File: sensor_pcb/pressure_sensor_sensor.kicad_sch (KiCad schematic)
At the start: 12 parts, among them J1 Conn_01x01_Pin, J10 Conn_01x02_Pin, J12 Conn_01x01_Pin, J13 Conn_01x01_Pin, J14 Conn_01x01_Pin, J15 Conn_01x01_Pin, J16 Conn_01x01_Pin, J17 Conn_01x01_Pin, J18 Conn_01x01_Pin, J7 Conn_01x02_Pin, J8 Conn_01x02_Pin, J9 Conn_01x02_Pin

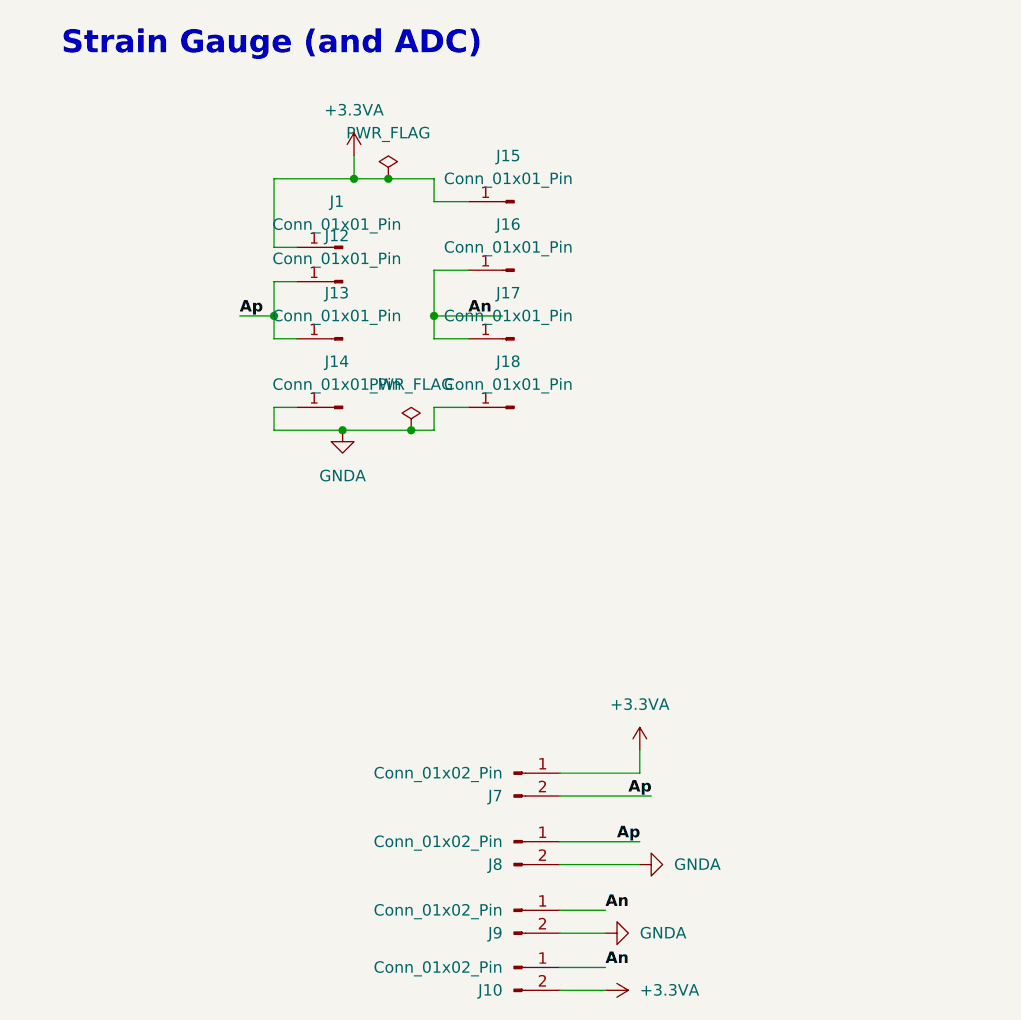
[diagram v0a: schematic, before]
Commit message: mounting_holes_added
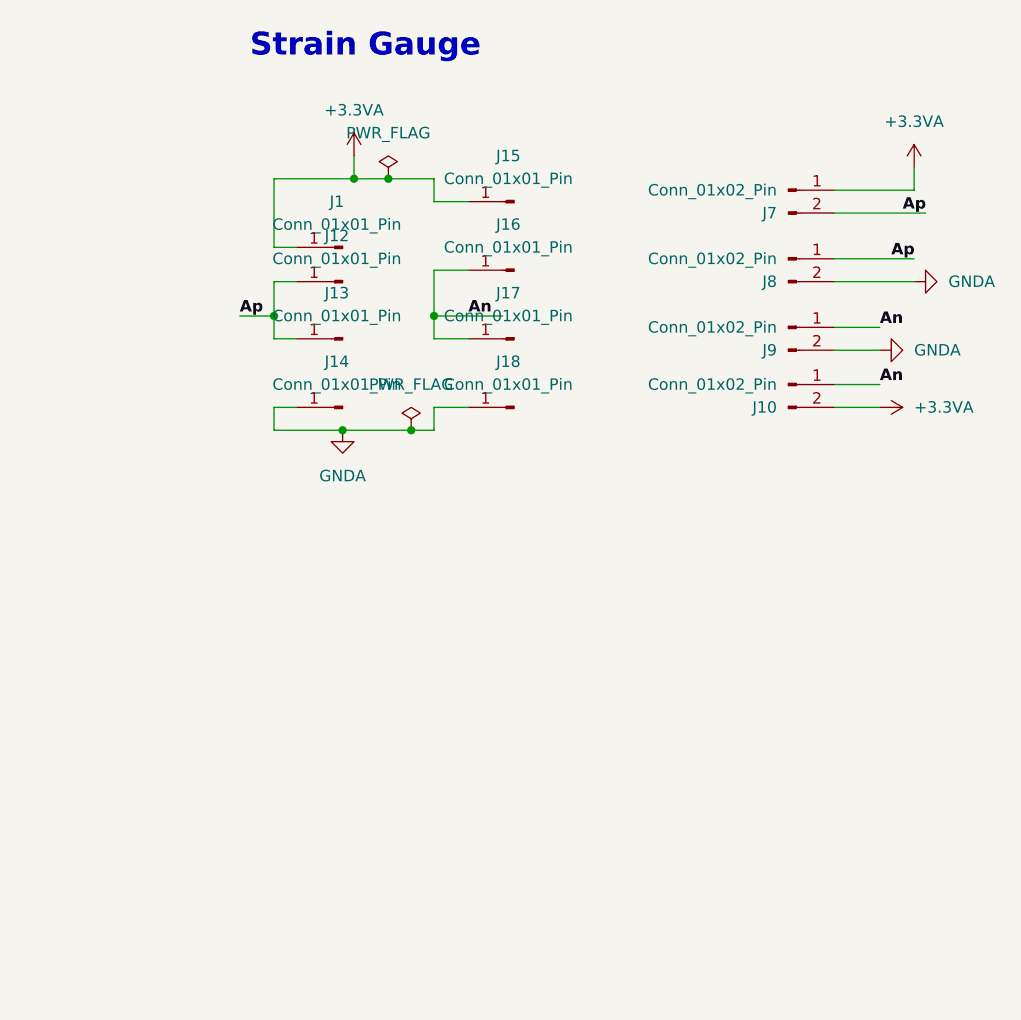
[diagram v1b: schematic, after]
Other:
- note added: "Strain Gauge"
- note removed: "Strain Gauge (and ADC)"
- moved on the sheet: J10, J7, J8, J9
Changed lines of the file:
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@@
 	(wire
 		(pts
-			(xy 205.74 97.79) (xy 214.63 97.79)
-		)
-		(stroke
-			(width 0)
-			(type default)
-		)
-	)
-	(wire
-		(pts
-			(xy 205.74 107.95) (xy 214.63 107.95)
+			(xy 236.22 33.02) (xy 245.11 33.02)
+		)
+		(stroke
+			(width 0)
+			(type default)
+		)
+	)
+	(wire
+		(pts
+			(xy 236.22 43.18) (xy 245.11 43.18)
 		)
 		(stroke
@@
 	(wire
 		(pts
-			(xy 205.74 100.33) (xy 215.9 100.33)
+			(xy 236.22 35.56) (xy 246.38 35.56)
 		)
 		(stroke
@@
 	(wire
 		(pts
-			(xy 205.74 105.41) (xy 214.63 105.41)
+			(xy 236.22 40.64) (xy 245.11 40.64)
 		)
 		(stroke
@@
 	(wire
 		(pts
-			(xy 205.74 115.57) (xy 210.82 115.57)
+			(xy 236.22 50.8) (xy 241.3 50.8)
 		)
 		(stroke
@@
 	(wire
 		(pts
-			(xy 205.74 113.03) (xy 210.82 113.03)
+			(xy 236.22 48.26) (xy 241.3 48.26)
 		)
 		(stroke
@@
 	(wire
 		(pts
-			(xy 205.74 121.92) (xy 210.82 121.92)
+			(xy 236.22 57.15) (xy 241.3 57.15)
 		)
 		(stroke
@@
 	(wire
 		(pts
-			(xy 205.74 119.38) (xy 210.82 119.38)
-		)
-		(stroke
-			(width 0)
-			(type default)
-		)
-	)
-	(wire
-		(pts
-			(xy 214.63 95.25) (xy 214.63 97.79)
-		)
-		(stroke
-			(width 0)
-			(type default)
-		)
-	)
-	(text "Strain Gauge (and ADC)"
-		(exclude_from_sim no)
-		(at 173.736 16.764 0)
+			(xy 236.22 54.61) (xy 241.3 54.61)
+		)
+		(stroke
+			(width 0)
+			(type default)
+		)
+	)
+	(wire
+		(pts
+			(xy 245.11 30.48) (xy 245.11 33.02)
+		)
+		(stroke
+			(width 0)
+			(type default)
+		)
+	)
+	(text "Strain Gauge"
+		(exclude_from_sim no)
+		(at 184.15 17.018 0)
 		(effects
 			(font
@@
 	)
 	(label "Ap"
-		(at 212.09 105.41 0)
+		(at 242.57 40.64 0)
 		(fields_autoplaced yes)
 		(effects
@@
 	)
 	(label "An"
-		(at 210.82 113.03 0)
+		(at 241.3 48.26 0)
 		(fields_autoplaced yes)
 		(effects
@@
 	)
 	(label "Ap"
-		(at 213.36 100.33 0)
+		(at 243.84 35.56 0)
 		(fields_autoplaced yes)
 		(effects
@@
 	)
 	(label "An"
-		(at 210.82 119.38 0)
+		(at 241.3 54.61 0)
 		(fields_autoplaced yes)
 		(effects
@@
 	(symbol
 		(lib_id "Connector:Conn_01x02_Pin")
-		(at 200.66 113.03 0)
+		(at 231.14 48.26 0)
 		(unit 1)
 		(exclude_from_sim no)
@@
 		(dnp no)
 		(property "Reference" "J9"
-			(at 199.39 115.5701 0)
+			(at 229.87 50.8001 0)
 			(effects
 				(font
@@
 		)
 		(property "Value" "Conn_01x02_Pin"
-			(at 199.39 113.0301 0)
+			(at 229.87 48.2601 0)
 			(effects
 				(font
@@
 		)
 		(property "Footprint" "Connector_PinHeader_1.00mm:PinHeader_1x02_P1.00mm_Vertical"
-			(at 200.66 113.03 0)
+			(at 231.14 48.26 0)
 			(effects
 				(font
@@
 		)
 		(property "Datasheet" "~"
-			(at 200.66 113.03 0)
+			(at 231.14 48.26 0)
 			(effects
 				(font
@@
 		)
 		(property "Description" "Generic connector, single row, 01x02, script generated"
-			(at 200.66 113.03 0)
+			(at 231.14 48.26 0)
 			(effects
 				(font
@@
 	(symbol
 		(lib_id "Connector:Conn_01x02_Pin")
-		(at 200.66 119.38 0)
+		(at 231.14 54.61 0)
 		(unit 1)
 		(exclude_from_sim no)
@@
 		(dnp no)
 		(property "Reference" "J10"
-			(at 199.39 121.9201 0)
+			(at 229.87 57.1501 0)
 			(effects
 				(font
@@
 		)
 		(property "Value" "Conn_01x02_Pin"
-			(at 199.39 119.3801 0)
+			(at 229.87 54.6101 0)
 			(effects
 				(font
@@
 		)
 		(property "Footprint" "Connector_PinHeader_1.00mm:PinHeader_1x02_P1.00mm_Vertical"
-			(at 200.66 119.38 0)
+			(at 231.14 54.61 0)
 			(effects
 				(font
@@
 		)
 		(property "Datasheet" "~"
-			(at 200.66 119.38 0)
+			(at 231.14 54.61 0)
 			(effects
 				(font
@@
 		)
 		(property "Description" "Generic connector, single row, 01x02, script generated"
-			(at 200.66 119.38 0)
+			(at 231.14 54.61 0)
 			(effects
 				(font
@@
 	(symbol
 		(lib_id "power:GNDA")
-		(at 210.82 115.57 90)
+		(at 241.3 50.8 90)
 		(unit 1)
 		(exclude_from_sim no)
@@
 		(fields_autoplaced yes)
 		(property "Reference" "#PWR016"
-			(at 217.17 115.57 0)
+			(at 247.65 50.8 0)
 			(effects
 				(font
@@
 		)
 		(property "Value" "GNDA"
-			(at 214.63 115.5699 90)
+			(at 245.11 50.7999 90)
 			(effects
 				(font
@@
 		)
 		(property "Footprint" ""
-			(at 210.82 115.57 0)
+			(at 241.3 50.8 0)
 			(effects
 				(font
@@
 		)
 		(property "Datasheet" ""
-			(at 210.82 115.57 0)
+			(at 241.3 50.8 0)
 			(effects
 				(font
@@
 		)
 		(property "Description" "Power symbol creates a global label with name \"GNDA\" , analog ground"
-			(at 210.82 115.57 0)
+			(at 241.3 50.8 0)
 			(effects
 				(font
@@
 	(symbol
 		(lib_id "Connector:Conn_01x02_Pin")
-		(at 200.66 97.79 0)
+		(at 231.14 33.02 0)
 		(unit 1)
 		(exclude_from_sim no)
@@
 		(dnp no)
 		(property "Reference" "J7"
-			(at 199.39 100.3301 0)
+			(at 229.87 35.5601 0)
 			(effects
 				(font
@@
 		)
 		(property "Value" "Conn_01x02_Pin"
-			(at 199.39 97.7901 0)
+			(at 229.87 33.0201 0)
 			(effects
 				(font
@@
 		)
 		(property "Footprint" "Connector_PinHeader_1.00mm:PinHeader_1x02_P1.00mm_Vertical"
-			(at 200.66 97.79 0)
+			(at 231.14 33.02 0)
 			(effects
 				(font
@@
 		)
 		(property "Datasheet" "~"
-			(at 200.66 97.79 0)
+			(at 231.14 33.02 0)
 			(effects
 				(font
@@
 		)
 		(property "Description" "Generic connector, single row, 01x02, script generated"
-			(at 200.66 97.79 0)
+			(at 231.14 33.02 0)
 			(effects
 				(font
@@
 	(symbol
 		(lib_id "power:GNDA")
-		(at 214.63 107.95 90)
+		(at 245.11 43.18 90)
 		(unit 1)
 		(exclude_from_sim no)
@@
 		(fields_autoplaced yes)
 		(property "Reference" "#PWR012"
-			(at 220.98 107.95 0)
+			(at 251.46 43.18 0)
 			(effects
 				(font
@@
 		)
 		(property "Value" "GNDA"
-			(at 218.44 107.9499 90)
+			(at 248.92 43.1799 90)
 			(effects
 				(font
@@
 		)
 		(property "Footprint" ""
-			(at 214.63 107.95 0)
+			(at 245.11 43.18 0)
 			(effects
 				(font
@@
 		)
 		(property "Datasheet" ""
-			(at 214.63 107.95 0)
+			(at 245.11 43.18 0)
 			(effects
 				(font
@@
 		)
 		(property "Description" "Power symbol creates a global label with name \"GNDA\" , analog ground"
-			(at 214.63 107.95 0)
+			(at 245.11 43.18 0)
 			(effects
 				(font
@@
 	(symbol
 		(lib_id "power:+3.3VA")
-		(at 214.63 95.25 0)
+		(at 245.11 30.48 0)
 		(unit 1)
 		(exclude_from_sim no)
@@
 		(fields_autoplaced yes)
 		(property "Reference" "#PWR09"
-			(at 214.63 99.06 0)
+			(at 245.11 34.29 0)
 			(effects
 				(font
@@
 		)
 		(property "Value" "+3.3VA"
-			(at 214.63 90.17 0)
+			(at 245.11 25.4 0)
 			(effects
 				(font
@@
 		)
 		(property "Footprint" ""
-			(at 214.63 95.25 0)
+			(at 245.11 30.48 0)
 			(effects
 				(font
@@
 		)
 		(property "Datasheet" ""
-			(at 214.63 95.25 0)
+			(at 245.11 30.48 0)
 			(effects
 				(font
@@
 		)
 		(property "Description" "Power symbol creates a global label with name \"+3.3VA\""
-			(at 214.63 95.25 0)
+			(at 245.11 30.48 0)
 			(effects
 				(font
@@
 	(symbol
 		(lib_id "power:+3.3VA")
-		(at 210.82 121.92 270)
+		(at 241.3 57.15 270)
 		(unit 1)
 		(exclude_from_sim no)
@@
 		(fields_autoplaced yes)
 		(property "Reference" "#PWR017"
-			(at 207.01 121.92 0)
+			(at 237.49 57.15 0)
 			(effects
 				(font
@@
 		)
 		(property "Value" "+3.3VA"
-			(at 214.63 121.9199 90)
+			(at 245.11 57.1499 90)
 			(effects
 				(font
@@
 		)
 		(property "Footprint" ""
-			(at 210.82 121.92 0)
+			(at 241.3 57.15 0)
 			(effects
 				(font
@@
 		)
 		(property "Datasheet" ""
-			(at 210.82 121.92 0)
+			(at 241.3 57.15 0)
 			(effects
 				(font
@@
 		)
 		(property "Description" "Power symbol creates a global label with name \"+3.3VA\""
-			(at 210.82 121.92 0)
+			(at 241.3 57.15 0)
 			(effects
 				(font
@@
 	(symbol
 		(lib_id "Connector:Conn_01x02_Pin")
-		(at 200.66 105.41 0)
+		(at 231.14 40.64 0)
 		(unit 1)
 		(exclude_from_sim no)
@@
 		(dnp no)
 		(property "Reference" "J8"
-			(at 199.39 107.9501 0)
+			(at 229.87 43.1801 0)
 			(effects
 				(font
@@
 		)
 		(property "Value" "Conn_01x02_Pin"
-			(at 199.39 105.4101 0)
+			(at 229.87 40.6401 0)
 			(effects
 				(font
@@
 		)
 		(property "Footprint" "Connector_PinHeader_1.00mm:PinHeader_1x02_P1.00mm_Vertical"
-			(at 200.66 105.41 0)
+			(at 231.14 40.64 0)
 			(effects
 				(font
@@
 		)
 		(property "Datasheet" "~"
-			(at 200.66 105.41 0)
+			(at 231.14 40.64 0)
 			(effects
 				(font
@@
 		)
 		(property "Description" "Generic connector, single row, 01x02, script generated"
-			(at 200.66 105.41 0)
-			(effects
-				(font
+			(at 231.14 40.64 0)
+			(effects
+				(font
